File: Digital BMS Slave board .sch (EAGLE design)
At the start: 247 parts, among them J1 S7B-PH-K, J10 S3B-PH-K, J2 S4B-PH-K, J3 S4B-PH-K, J4 S6B-PH-K, J5 S2B-PH-K, J6 S2B-PH-K, J7 S2B-PH-K, J8 S2B-PH-K, J9 S3B-PH-K, Q1 BSS123, Q2 BSS123, Q3 BSS123, Q4 BSS123, Q5 BSS123, Q6 BSS123, X1 BQ79606A-Q1-HTQFP(PHP)|48, X2 PESD2CAN, X3 PESD2CAN, X4 PESD2CAN, X5 PESD2CAN

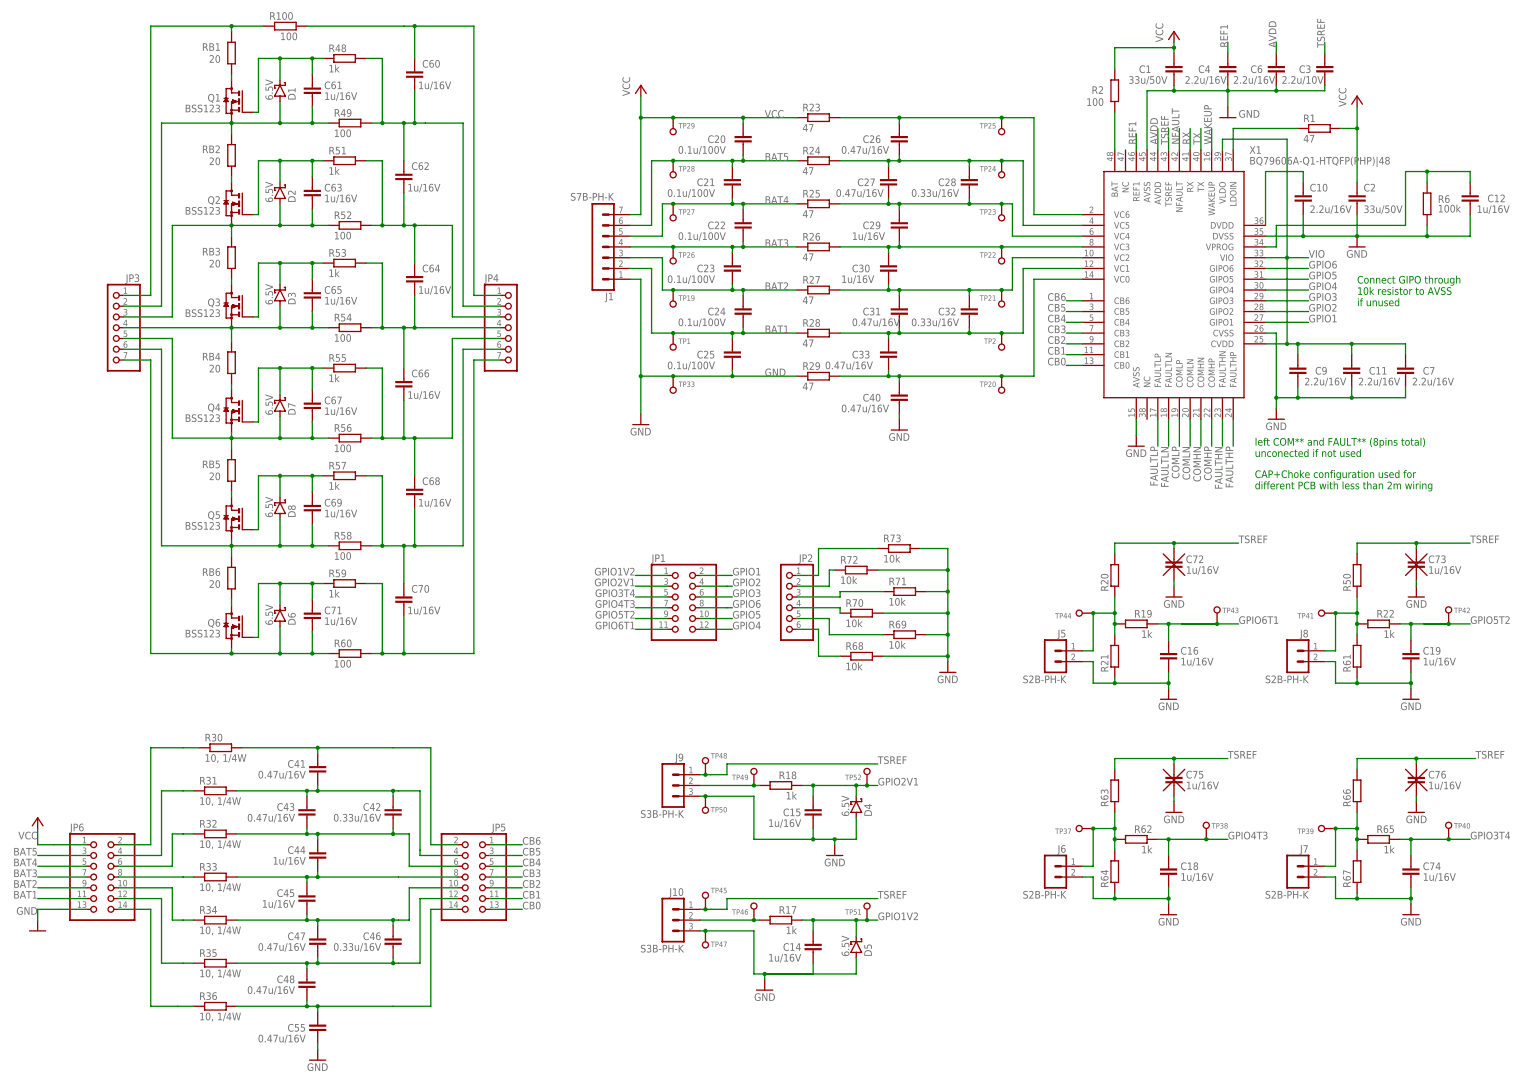
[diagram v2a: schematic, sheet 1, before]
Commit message: Schematic in accordance with BOM
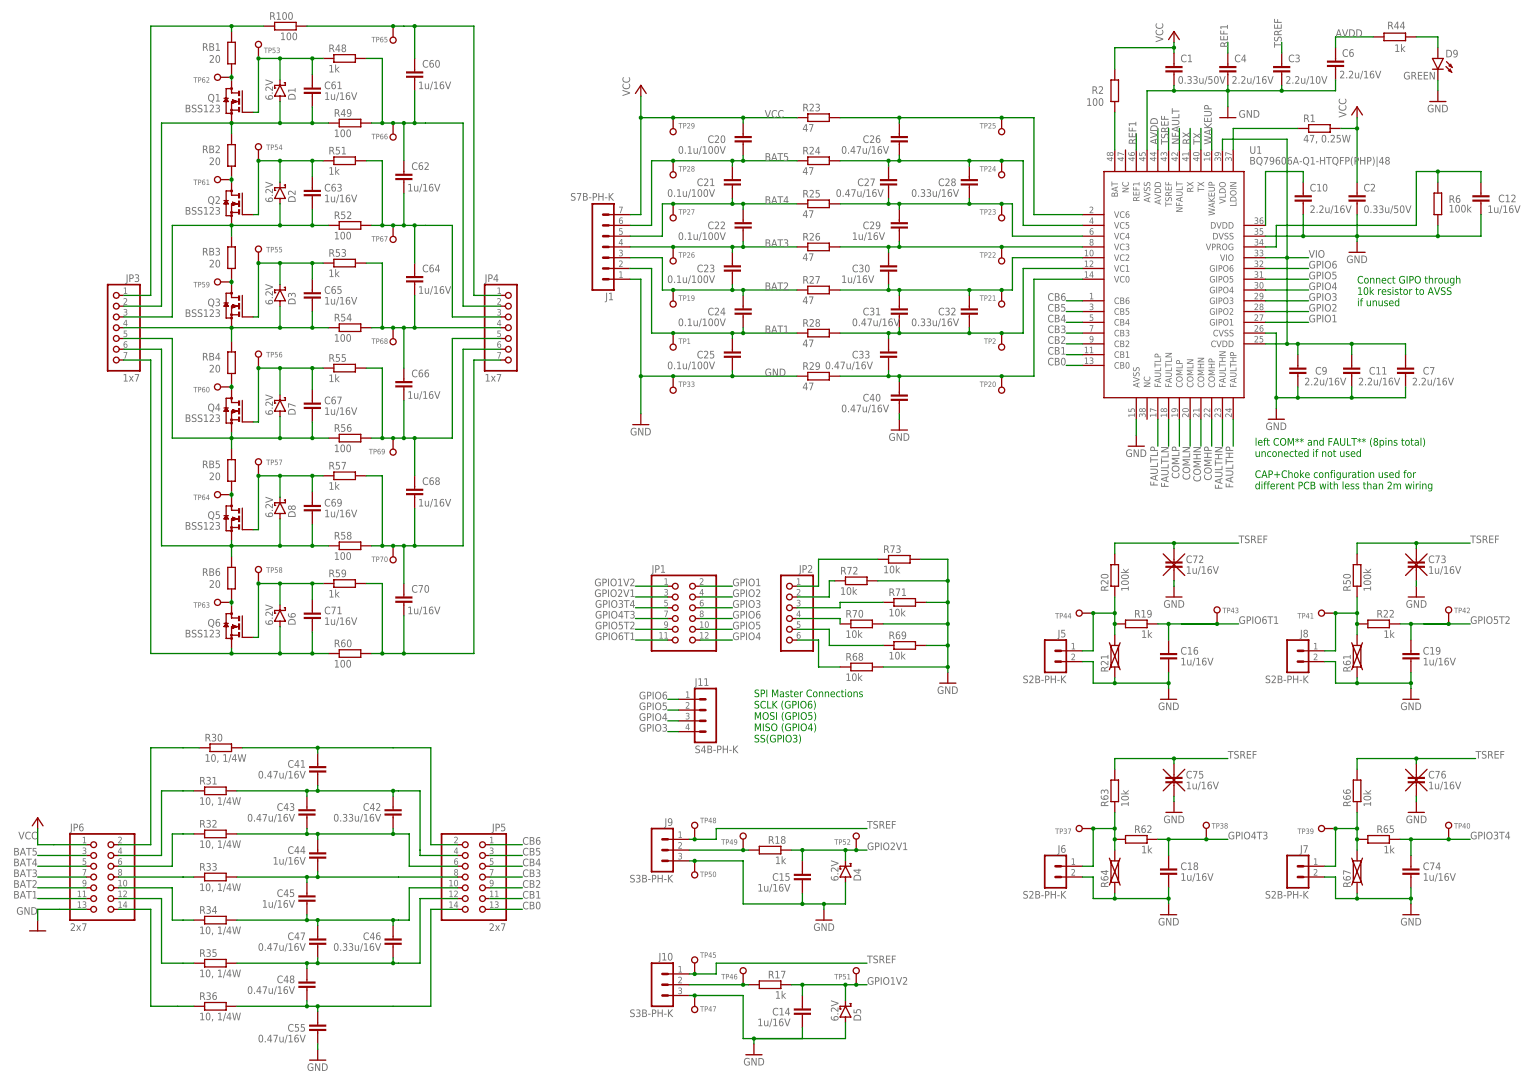
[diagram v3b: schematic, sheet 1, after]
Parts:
- added D9: GREEN, Semiconductor_devices:LED0805
- added J11: S4B-PH-K, con-jst-ph:S4B-PH-K
- added R74: 100, resistor:R-EU_R0603
- added TP53, TP54, TP55, TP56, TP57, TP58, TP59, TP60, TP61, TP62, TP63, TP64, TP65, TP66, TP67, TP68, TP69, TP70: TEST_PAD1, testing:TEST_PAD1
- C1, C2: value 33u/50V -> 0.33u/50V; device resistor:C-EUC0603 -> Capacitors:C-EU-K1206
- C13, C34, C37, C38, C50, C51, C54, C56: value 2200p -> 2.2n; device resistor:C-EUC0603 -> Capacitors:C-EU-K1206
- C20, C21, C22, C23, C24, C25: device resistor:C-EUC0603 -> Capacitors:C-EU-K1206
- C29, C30, C44, C45: device resistor:C-EUC0603 -> Capacitors:C-EU-K0805
- D1, D2, D3, D4, D5, D6, D7, D8: value 6.5V -> 6.2V
- JP3, JP4: value (none) -> 1x7
- JP5, JP6: value (none) -> 2x7
- R1: value 47 -> 47, 0.25W; device resistor:R-EU_R0603 -> Resistors:R-EU1206
- R20, R50: value (none) -> 100k
- R21, R61, R64, R67: device Resistors:R-EU0603 -> Resistors:R-EU-X0603
- R44: value 100k -> 1k; device resistor:R-EU_R0603 -> Resistors:R-EU0603
- R45, R46, R47: value 100k -> 10k
- R6: device resistor:R-EU_R0603 -> Resistors:R-EU0603
- R63, R66: value (none) -> 10k
- renumbered X1 to U1
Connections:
- new net N$28: D9.A, R44.1
- new net RX1: C57.2, J4.3, R47.1, R74.1, TP32.P$1
- net AVDD: now also R44.2
- net GND: now also D9.C
- net GPIO3: now also J11.4
- net GPIO4: now also J11.3
- net GPIO5: now also J11.2
- net GPIO6: now also J11.1
- net N$22: now also TP59.P$1
- net N$3: now also TP62.P$1
- net N$30: now also TP53.P$1
- net N$31: now also TP61.P$1
- net N$33: now also TP66.P$1
- net N$34: now also TP64.P$1
- net N$6: now also TP65.P$1
- net N$60: now also TP54.P$1
- net N$61: now also TP67.P$1
- net N$62: now also TP55.P$1
- net N$63: now also TP60.P$1
- net N$65: now also TP68.P$1
- net N$66: now also TP69.P$1
- net N$68: now also TP56.P$1
- net N$70: now also TP57.P$1
- net N$71: now also TP63.P$1
- net N$73: now also TP70.P$1
- net N$76: now also TP58.P$1
- net RX: now also R74.2; no longer C57.2, J4.3, R47.1, TP32.P$1
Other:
- note added: "SPI Master Connections SCLK (GPIO6) MOSI (GPIO5) MISO (GPIO4) SS(GPIO3)"
- note removed: "remeber about TX pull up resistor on the other side (isolator board)"
- moved on the sheet: C12, C14, C15, C3, C6, D4, D5, J10, J9, JP1, JP2, R17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

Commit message: Footprint fixed
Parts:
- R30, R31, R32, R33, R34, R35, R36: device resistor:R-EU_R0603 -> resistor:R-EU_R1210
- RB1, RB2, RB3, RB4, RB5, RB6: device resistor:R-EU_R0603 -> Resistors:R-EU2512
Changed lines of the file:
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@@
 <part name="C60" library="resistor" library_urn="urn:adsk.eagle:library:348" deviceset="C-EU" device="C0603" package3d_urn="urn:adsk.eagle:package:23616/2" value="1u/16V"/>
 <part name="R100" library="resistor" library_urn="urn:adsk.eagle:library:348" deviceset="R-EU_" device="R0603" package3d_urn="urn:adsk.eagle:package:23555/3" value="100"/>
-<part name="RB1" library="resistor" library_urn="urn:adsk.eagle:library:348" deviceset="R-EU_" device="R0603" package3d_urn="urn:adsk.eagle:package:23555/3" value="20"/>
+<part name="RB1" library="Resistors" library_urn="urn:adsk.eagle:library:13360588" deviceset="R-EU" device="2512" package3d_urn="urn:adsk.eagle:package:23545/2" value="20"/>
 <part name="Q1" library="transistor-small-signal" library_urn="urn:adsk.eagle:library:401" deviceset="BSS123" device="" package3d_urn="urn:adsk.eagle:package:28738/2"/>
 <part name="C61" library="resistor" library_urn="urn:adsk.eagle:library:348" deviceset="C-EU" device="C0603" package3d_urn="urn:adsk.eagle:package:23616/2" value="1u/16V"/>
@@
 <part name="R49" library="resistor" library_urn="urn:adsk.eagle:library:348" deviceset="R-EU_" device="R0603" package3d_urn="urn:adsk.eagle:package:23555/3" value="100"/>
 <part name="C62" library="resistor" library_urn="urn:adsk.eagle:library:348" deviceset="C-EU" device="C0603" package3d_urn="urn:adsk.eagle:package:23616/2" value="1u/16V"/>
-<part name="RB2" library="resistor" library_urn="urn:adsk.eagle:library:348" deviceset="R-EU_" device="R0603" package3d_urn="urn:adsk.eagle:package:23555/3" value="20"/>
+<part name="RB2" library="Resistors" library_urn="urn:adsk.eagle:library:13360588" deviceset="R-EU" device="2512" package3d_urn="urn:adsk.eagle:package:23545/2" value="20"/>
 <part name="Q2" library="transistor-small-signal" library_urn="urn:adsk.eagle:library:401" deviceset="BSS123" device="" package3d_urn="urn:adsk.eagle:package:28738/2"/>
 <part name="C63" library="resistor" library_urn="urn:adsk.eagle:library:348" deviceset="C-EU" device="C0603" package3d_urn="urn:adsk.eagle:package:23616/2" value="1u/16V"/>
@@
 <part name="R52" library="resistor" library_urn="urn:adsk.eagle:library:348" deviceset="R-EU_" device="R0603" package3d_urn="urn:adsk.eagle:package:23555/3" value="100"/>
 <part name="C64" library="resistor" library_urn="urn:adsk.eagle:library:348" deviceset="C-EU" device="C0603" package3d_urn="urn:adsk.eagle:package:23616/2" value="1u/16V"/>
-<part name="RB3" library="resistor" library_urn="urn:adsk.eagle:library:348" deviceset="R-EU_" device="R0603" package3d_urn="urn:adsk.eagle:package:23555/3" value="20"/>
+<part name="RB3" library="Resistors" library_urn="urn:adsk.eagle:library:13360588" deviceset="R-EU" device="2512" package3d_urn="urn:adsk.eagle:package:23545/2" value="20"/>
 <part name="Q3" library="transistor-small-signal" library_urn="urn:adsk.eagle:library:401" deviceset="BSS123" device="" package3d_urn="urn:adsk.eagle:package:28738/2"/>
 <part name="C65" library="resistor" library_urn="urn:adsk.eagle:library:348" deviceset="C-EU" device="C0603" package3d_urn="urn:adsk.eagle:package:23616/2" value="1u/16V"/>
@@
 <part name="R54" library="resistor" library_urn="urn:adsk.eagle:library:348" deviceset="R-EU_" device="R0603" package3d_urn="urn:adsk.eagle:package:23555/3" value="100"/>
 <part name="C66" library="resistor" library_urn="urn:adsk.eagle:library:348" deviceset="C-EU" device="C0603" package3d_urn="urn:adsk.eagle:package:23616/2" value="1u/16V"/>
-<part name="RB4" library="resistor" library_urn="urn:adsk.eagle:library:348" deviceset="R-EU_" device="R0603" package3d_urn="urn:adsk.eagle:package:23555/3" value="20"/>
+<part name="RB4" library="Resistors" library_urn="urn:adsk.eagle:library:13360588" deviceset="R-EU" device="2512" package3d_urn="urn:adsk.eagle:package:23545/2" value="20"/>
 <part name="Q4" library="transistor-small-signal" library_urn="urn:adsk.eagle:library:401" deviceset="BSS123" device="" package3d_urn="urn:adsk.eagle:package:28738/2"/>
 <part name="C67" library="resistor" library_urn="urn:adsk.eagle:library:348" deviceset="C-EU" device="C0603" package3d_urn="urn:adsk.eagle:package:23616/2" value="1u/16V"/>
@@
 <part name="R56" library="resistor" library_urn="urn:adsk.eagle:library:348" deviceset="R-EU_" device="R0603" package3d_urn="urn:adsk.eagle:package:23555/3" value="100"/>
 <part name="C68" library="resistor" library_urn="urn:adsk.eagle:library:348" deviceset="C-EU" device="C0603" package3d_urn="urn:adsk.eagle:package:23616/2" value="1u/16V"/>
-<part name="RB5" library="resistor" library_urn="urn:adsk.eagle:library:348" deviceset="R-EU_" device="R0603" package3d_urn="urn:adsk.eagle:package:23555/3" value="20"/>
+<part name="RB5" library="Resistors" library_urn="urn:adsk.eagle:library:13360588" deviceset="R-EU" device="2512" package3d_urn="urn:adsk.eagle:package:23545/2" value="20"/>
 <part name="Q5" library="transistor-small-signal" library_urn="urn:adsk.eagle:library:401" deviceset="BSS123" device="" package3d_urn="urn:adsk.eagle:package:28738/2"/>
 <part name="C69" library="resistor" library_urn="urn:adsk.eagle:library:348" deviceset="C-EU" device="C0603" package3d_urn="urn:adsk.eagle:package:23616/2" value="1u/16V"/>
@@
 <part name="R58" library="resistor" library_urn="urn:adsk.eagle:library:348" deviceset="R-EU_" device="R0603" package3d_urn="urn:adsk.eagle:package:23555/3" value="100"/>
 <part name="C70" library="resistor" library_urn="urn:adsk.eagle:library:348" deviceset="C-EU" device="C0603" package3d_urn="urn:adsk.eagle:package:23616/2" value="1u/16V"/>
-<part name="RB6" library="resistor" library_urn="urn:adsk.eagle:library:348" deviceset="R-EU_" device="R0603" package3d_urn="urn:adsk.eagle:package:23555/3" value="20"/>
+<part name="RB6" library="Resistors" library_urn="urn:adsk.eagle:library:13360588" deviceset="R-EU" device="2512" package3d_urn="urn:adsk.eagle:package:23545/2" value="20"/>
 <part name="Q6" library="transistor-small-signal" library_urn="urn:adsk.eagle:library:401" deviceset="BSS123" device="" package3d_urn="urn:adsk.eagle:package:28738/2"/>
 <part name="C71" library="resistor" library_urn="urn:adsk.eagle:library:348" deviceset="C-EU" device="C0603" package3d_urn="urn:adsk.eagle:package:23616/2" value="1u/16V"/>
@@
 <part name="TP21" library="testing" library_urn="urn:adsk.eagle:library:13096589" deviceset="TEST_PAD" device="2" package3d_urn="urn:adsk.eagle:package:13096604/2"/>
 <part name="TP27" library="testing" library_urn="urn:adsk.eagle:library:13096589" deviceset="TEST_PAD" device="2" package3d_urn="urn:adsk.eagle:package:13096604/2"/>
-<part name="R30" library="resistor" library_urn="urn:adsk.eagle:library:348" deviceset="R-EU_" device="R0603" package3d_urn="urn:adsk.eagle:package:23555/3" value="10, 1/4W"/>
-<part name="R31" library="resistor" library_urn="urn:adsk.eagle:library:348" deviceset="R-EU_" device="R0603" package3d_urn="urn:adsk.eagle:package:23555/3" value="10, 1/4W"/>
-<part name="R32" library="resistor" library_urn="urn:adsk.eagle:library:348" deviceset="R-EU_" device="R0603" package3d_urn="urn:adsk.eagle:package:23555/3" value="10, 1/4W"/>
-<part name="R33" library="resistor" library_urn="urn:adsk.eagle:library:348" deviceset="R-EU_" device="R0603" package3d_urn="urn:adsk.eagle:package:23555/3" value="10, 1/4W"/>
-<part name="R34" library="resistor" library_urn="urn:adsk.eagle:library:348" deviceset="R-EU_" device="R0603" package3d_urn="urn:adsk.eagle:package:23555/3" value="10, 1/4W"/>
-<part name="R35" library="resistor" library_urn="urn:adsk.eagle:library:348" deviceset="R-EU_" device="R0603" package3d_urn="urn:adsk.eagle:package:23555/3" value="10, 1/4W"/>
-<part name="R36" library="resistor" library_urn="urn:adsk.eagle:library:348" deviceset="R-EU_" device="R0603" package3d_urn="urn:adsk.eagle:package:23555/3" value="10, 1/4W"/>
+<part name="R30" library="resistor" library_urn="urn:adsk.eagle:library:348" deviceset="R-EU_" device="R1210" package3d_urn="urn:adsk.eagle:package:23554/2" value="10, 1/4W"/>
+<part name="R31" library="resistor" library_urn="urn:adsk.eagle:library:348" deviceset="R-EU_" device="R1210" package3d_urn="urn:adsk.eagle:package:23554/2" value="10, 1/4W"/>
+<part name="R32" library="resistor" library_urn="urn:adsk.eagle:library:348" deviceset="R-EU_" device="R1210" package3d_urn="urn:adsk.eagle:package:23554/2" value="10, 1/4W"/>
+<part name="R33" library="resistor" library_urn="urn:adsk.eagle:library:348" deviceset="R-EU_" device="R1210" package3d_urn="urn:adsk.eagle:package:23554/2" value="10, 1/4W"/>
+<part name="R34" library="resistor" library_urn="urn:adsk.eagle:library:348" deviceset="R-EU_" device="R1210" package3d_urn="urn:adsk.eagle:package:23554/2" value="10, 1/4W"/>
+<part name="R35" library="resistor" library_urn="urn:adsk.eagle:library:348" deviceset="R-EU_" device="R1210" package3d_urn="urn:adsk.eagle:package:23554/2" value="10, 1/4W"/>
+<part name="R36" library="resistor" library_urn="urn:adsk.eagle:library:348" deviceset="R-EU_" device="R1210" package3d_urn="urn:adsk.eagle:package:23554/2" value="10, 1/4W"/>
 <part name="C43" library="resistor" library_urn="urn:adsk.eagle:library:348" deviceset="C-EU" device="C0603" package3d_urn="urn:adsk.eagle:package:23616/2" value="0.47u/16V"/>
 <part name="C44" library="Capacitors" library_urn="urn:adsk.eagle:library:13360199" deviceset="C-EU-K" device="0805" package3d_urn="urn:adsk.eagle:package:13360230/1" value="1u/16V"/>
